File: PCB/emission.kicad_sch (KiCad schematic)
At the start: 6 parts, among them Q1 BSS138, U5 MCP6022

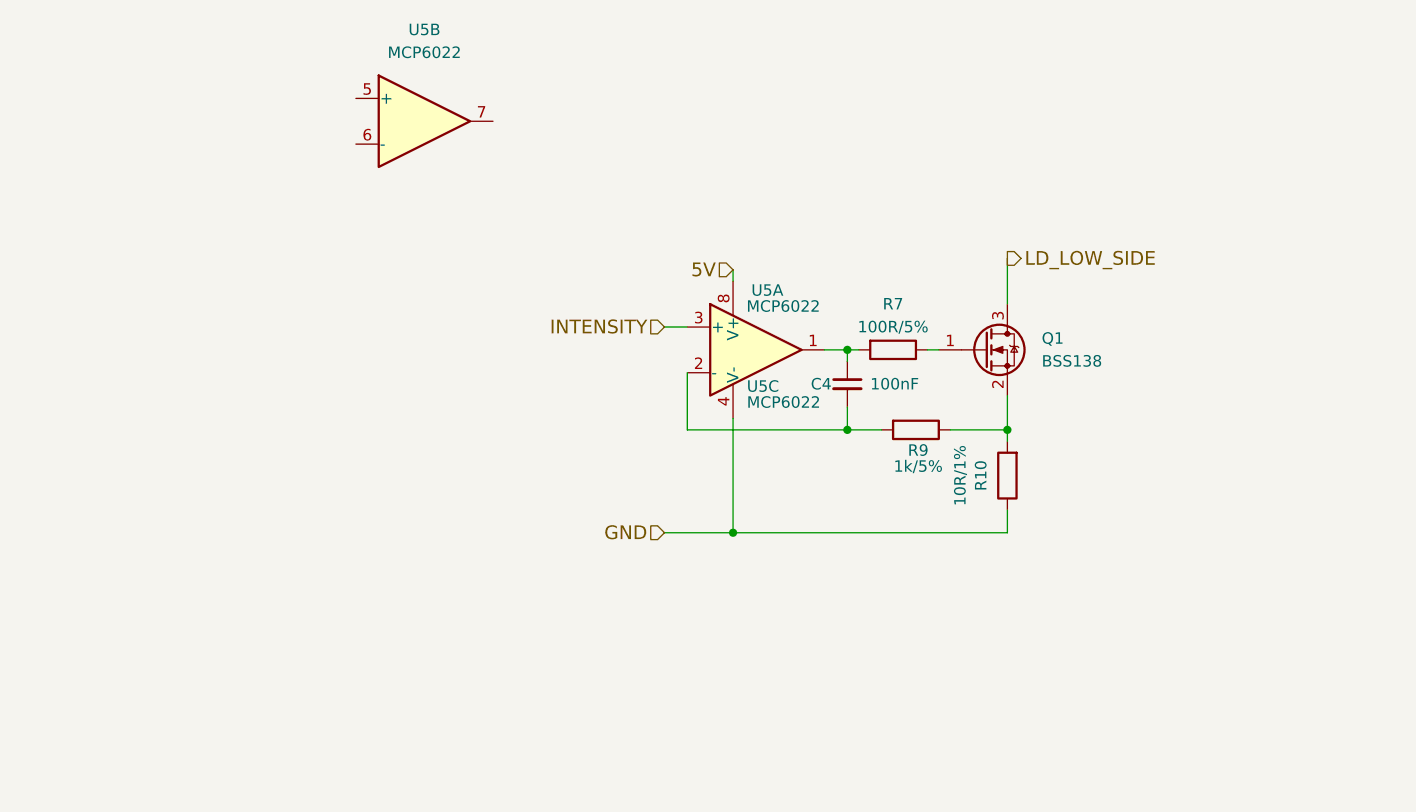
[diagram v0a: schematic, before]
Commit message: Update schematic based on testing
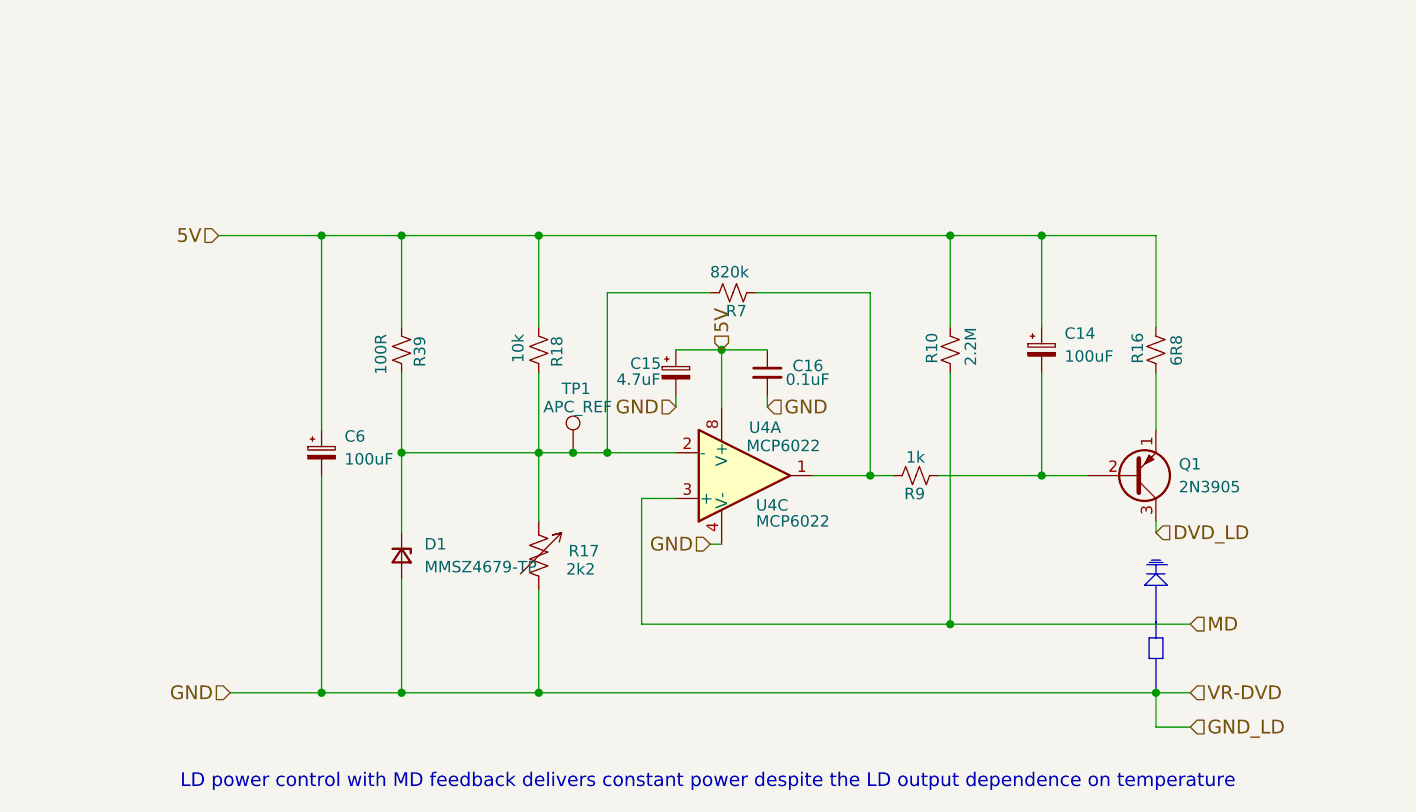
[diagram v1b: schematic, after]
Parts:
- removed C4: 100nF, GaudiLabsFootPrints:0805G, symbol DVDLaserScanner-rescue:C_Small
- removed Q1: BSS138, Package_TO_SOT_SMD:SOT-23, symbol Transistor_FET:BSS138
- removed R10: 10R/1%, GaudiLabsFootPrints:0805G, symbol DVDLaserScanner-rescue:R
- removed R7: 100R/5%, GaudiLabsFootPrints:0805G, symbol DVDLaserScanner-rescue:R
- removed R9: 1k/5%, GaudiLabsFootPrints:0805G, symbol DVDLaserScanner-rescue:R
- removed U5: MCP6022, symbol Amplifier_Operational:MCP6022
- added C14, C6: 100uF, symbol DVDLaserScanner-rescue:CP_Small
- added C15: 4.7uF, symbol DVDLaserScanner-rescue:CP_Small
- added C16: 0.1uF, symbol DVDLaserScanner-rescue:C_Small
- added D1: MMSZ4679-TP, Diode_SMD:D_SOD-123, symbol Device:D_Zener_Small
- added Q1: 2N3905, Package_TO_SOT_THT:TO-92_Inline, symbol Transistor_BJT:2N3905
- added R10: 2.2M, symbol Device:R_Small_US
- added R16: 6R8, symbol Device:R_Small_US
- added R17: 2k2, symbol Device:R_Variable_US
- added R18: 10k, symbol Device:R_Small_US
- added R39: 100R, symbol Device:R_Small_US
- added R7: 820k, symbol Device:R_Small_US
- added R9: 1k, symbol Device:R_Small_US
- added TP1: APC_REF, symbol Connector:TestPoint
- added U4: MCP6022, symbol Amplifier_Operational:MCP6022
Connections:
- net 5V: now also C14.1, C15.1, C16.1, C6.1, R10.1, R16.1, R18.2, R39.2, U4.8 (V+)
- net GND: now also C15.2, C16.2, C6.2, D1.2 (A), R17.2, U4.4 (V-)
- new net: Q1.1 (E), R16.2
- new net: C14.2, Q1.2 (B), R9.2
- new net: D1.1 (K), R17.1, R18.1, R39.1, R7.1, TP1.1, U4.2 (-)
- new net: R7.2, R9.1, U4.1
- new net DVD_LD: Q1.3 (C)
- new net MD: R10.2, U4.3 (+)
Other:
- note added: "LD power control with MD feedback delivers constant power despite the LD output dependence on temperature"
